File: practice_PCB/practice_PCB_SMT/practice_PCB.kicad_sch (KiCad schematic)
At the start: 22 parts, among them J1 5V, J2 GND

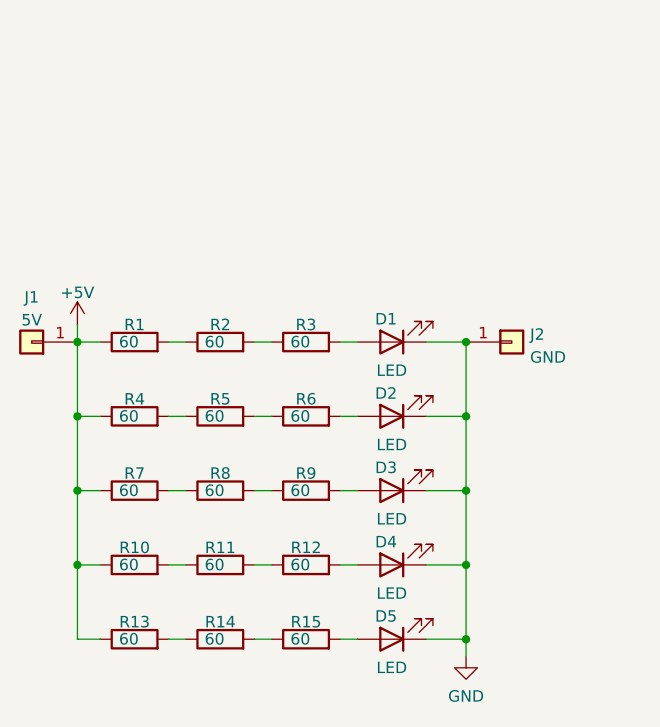
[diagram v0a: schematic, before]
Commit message: change the page layout and export to a pdf file
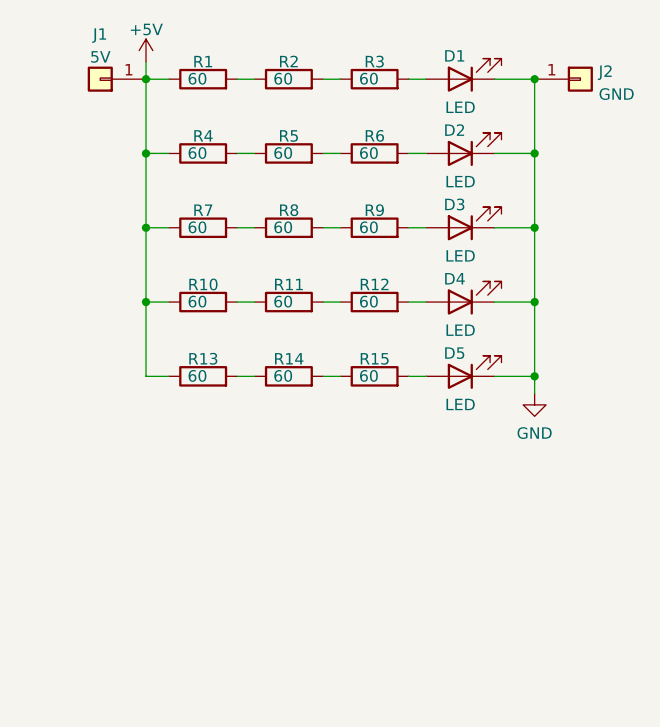
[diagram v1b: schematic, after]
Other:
- company: (none) -> Netz39 e.V.
- title: (none) -> Übungs-Lötset-SMT
- moved on the sheet: D1, D2, D3, D4, D5, J1, J2, R1, R10, R11, R12, R13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
